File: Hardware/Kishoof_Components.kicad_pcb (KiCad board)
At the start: 4 copper layers, 70.8 x 100 mm, 98 parts, among them J1 Conn_01x12_Pin, J2 Conn_01x12_Pin, J3 Conn_01x12_Pin, J4 Conn_01x12_Pin, J5 Eurorack_10_pin_power, J6 SWD_Header, J7 Conn_01x02_Pin, U1 STM32H7B0VBTx, U2 PCM5100APW, U3 TPS561201, U4 LT1117-3.3, U5 MCP6002, U6 MX25LM51245G, U7 MCP6004, U8 TL072, Y1 8MHz 20pF

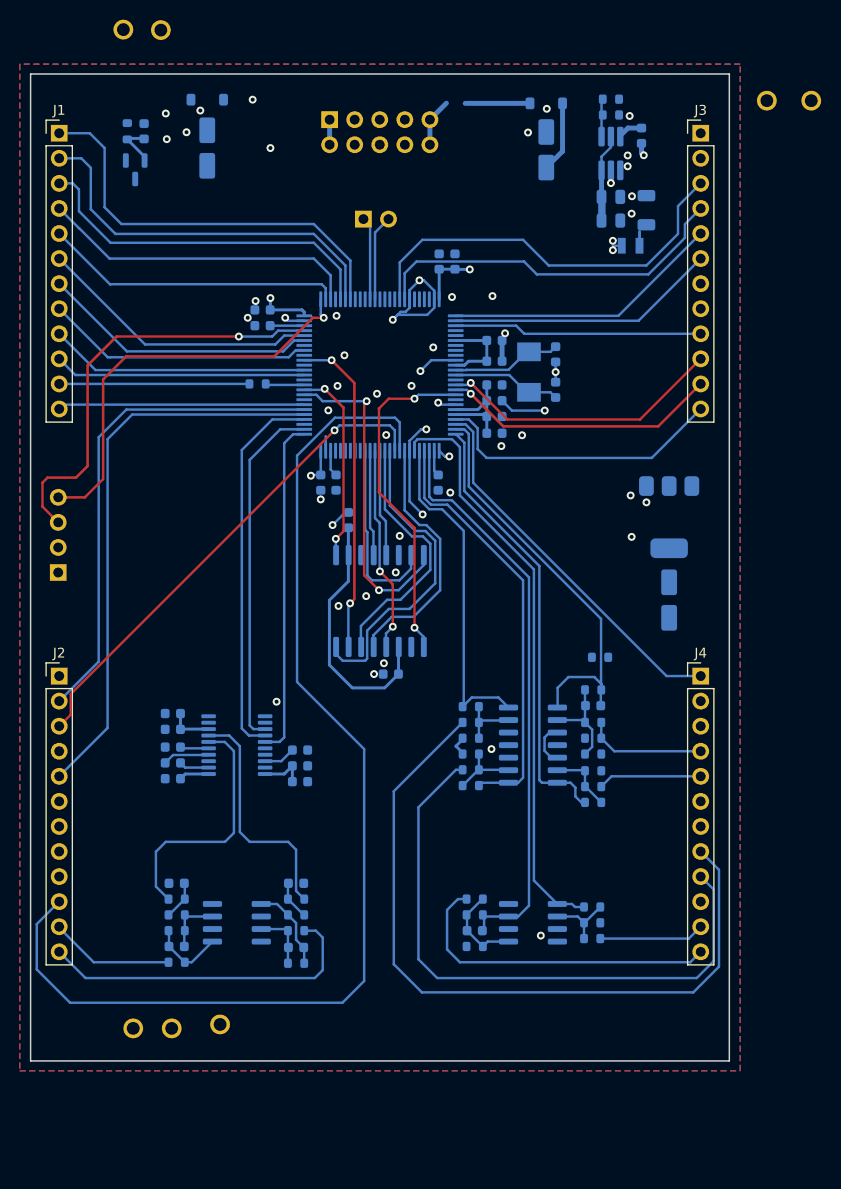
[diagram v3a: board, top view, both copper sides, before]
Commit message: First pass of component board routing complete
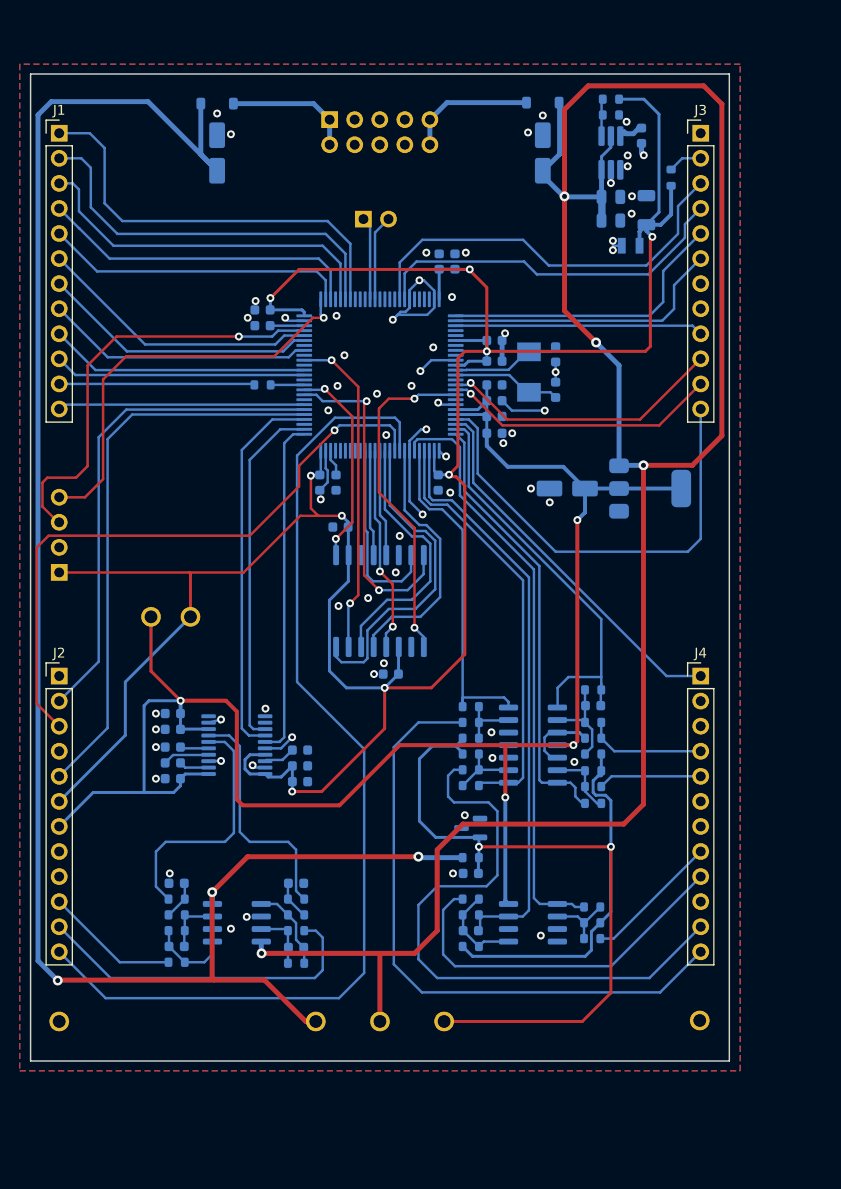
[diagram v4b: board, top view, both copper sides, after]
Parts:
- moved TP8 116.1 mm to (122.9, 134.9)
- moved TP3 105.9 mm to (84.0, 135.0)
- moved TP2 102.9 mm to (90.5, 135.0)
- moved TP7 98.9 mm to (97.0, 135.0)
- moved C36 82.2 mm to (99.7, 120.0), turned to 0 degrees
- moved R14 81.4 mm to (99.7, 118.4), turned to 0 degrees
- moved D3 74.9 mm to (99.7, 115.4), turned to 180 degrees
- moved R15 49.1 mm to (120.0, 49.5), turned to 90 degrees
- moved TP5 41.7 mm to (71.3, 94.0)
- moved TP6 41.7 mm to (67.3, 94.0)
- moved TP4 16.3 mm to (58.0, 135.0)
- moved C5 15.3 mm to (109.5, 81.0), turned to 180 degrees
- moved U4 3.48 mm to (117.9, 81.0), turned to 0 degrees
- moved C2 1.12 mm to (74.0, 47.0)
- moved D2 1.08 mm to (74.0, 42.0)
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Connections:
- J2 pad 1: unconnected-(J2-Pin_1-Pad1) -> GND
- J2 pad 10: /Warp_Type_Pot -> /Audio_Out_L
- J2 pad 11: /Audio_Out_L -> /Audio_Out_R
- J2 pad 12: /Audio_Out_R -> /Warp_Type_Pot
- J2 pad 4: unconnected-(J2-Pin_4-Pad4) -> GND
- J2 pad 6: GND -> +3.3V
- J2 pad 8: unconnected-(J2-Pin_8-Pad8) -> GND
- J2 pad 9: unconnected-(J2-Pin_9-Pad9) -> GND
- J3 pad 1: unconnected-(J3-Pin_1-Pad1) -> GND
- J3 pad 2: unconnected-(J3-Pin_2-Pad2) -> /LCD_Backlight
- J3 pad 7: unconnected-(J3-Pin_7-Pad7) -> GND
- J3 pad 8: unconnected-(J3-Pin_8-Pad8) -> GND
- J4 pad 10: unconnected-(J4-Pin_10-Pad10) -> GND
- J4 pad 11: /Wavetable_Pos_A_CV_In -> /Wavetable_Pos_B_CV_In
- J4 pad 12: /Pitch_CV_In -> /VCA_CV_In
- J4 pad 2: unconnected-(J4-Pin_2-Pad2) -> GND
- J4 pad 3: /LCD_Backlight -> GND
- J4 pad 6: +3.3V -> GND
- J4 pad 7: unconnected-(J4-Pin_7-Pad7) -> GND
- J4 pad 8: /VCA_CV_In -> /Wavetable_Pos_A_CV_In
- J4 pad 9: /Wavetable_Pos_B_CV_In -> /Pitch_CV_In
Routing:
- net +3.3V: track 58.2 -> 275.1 mm, vias 3 -> 9
- net +12V: track 15.7 -> 216.7 mm, vias 0 -> 4
- net -12V: track 0.00 -> 182.6 mm, vias 0 -> 3
- net +3.3VA: track 19.5 -> 177.7 mm, vias 0 -> 4
- net /-5V_REF: track 6.91 -> 105.8 mm, vias 0 -> 2
- net /Wavetable_Pos_B_Pot: track 29.7 -> 46.8 mm
- net /Wavetable_Pos_A_Pot: track 50.1 -> 63.9 mm
- net /VCA_CV_In: track 75.0 -> 64.0 mm
- net GND: track 50.1 -> 61.1 mm, vias 53 -> 63
- net /-12V_IN: track 2.54 -> 13.0 mm
- net /Warp_Type_Pot: track 114.4 -> 104.2 mm
- net /Pitch_CV_In: track 33.1 -> 37.3 mm
- net /LCD_Backlight: track 0.00 -> 3.47 mm
- net /Wavetable_Pos_A_CV_In: track 10.7 -> 13.8 mm
- net /Mode: track 28.3 -> 30.1 mm
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
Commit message: Cleaned up inter-board connectors
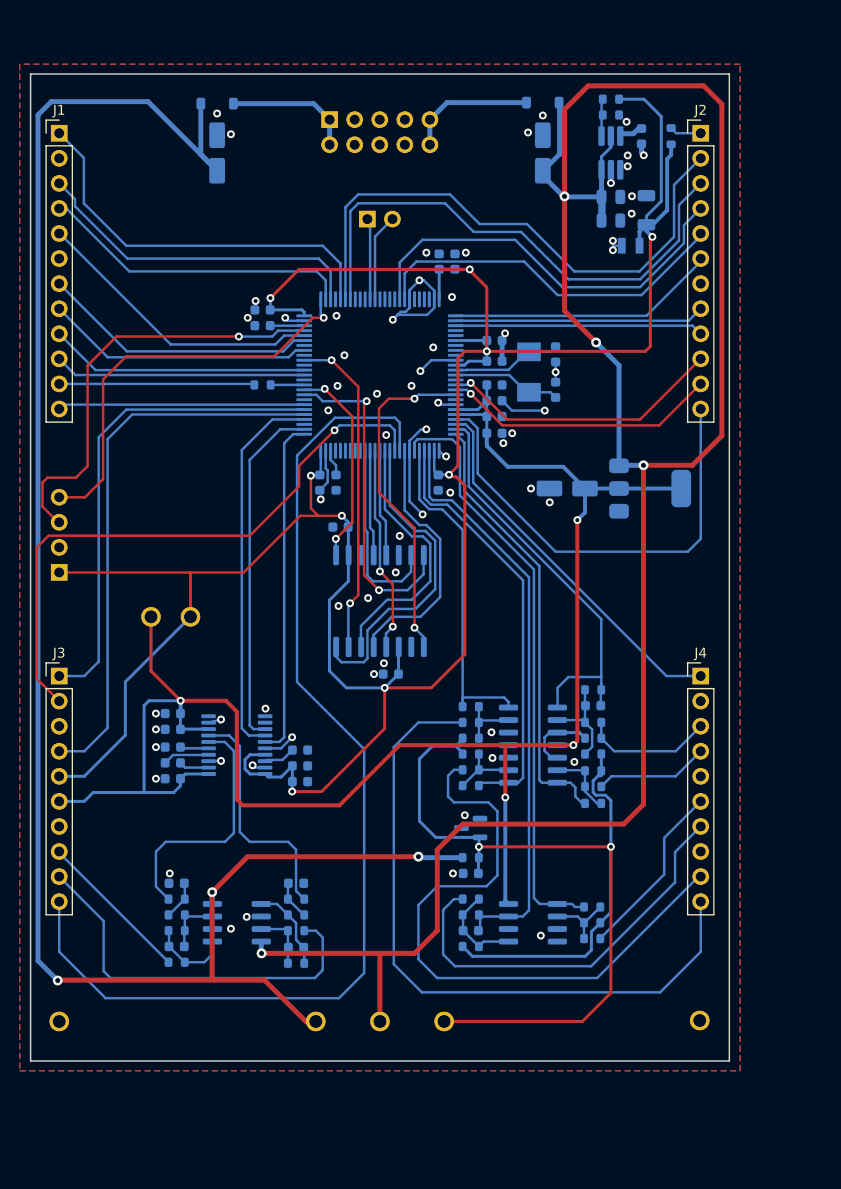
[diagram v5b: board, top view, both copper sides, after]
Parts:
- J3: renamed from J2; value Conn_01x12_Pin -> Conn_01x10_Pin; footprint Connector_PinHeader_2.54mm:PinHeader_1x12_P2.54mm_Vertical -> Connector_PinHeader_2.54mm:PinHeader_1x10_P2.54mm_Vertical
- J4: value Conn_01x12_Pin -> Conn_01x10_Pin; footprint Connector_PinHeader_2.54mm:PinHeader_1x12_P2.54mm_Vertical -> Connector_PinHeader_2.54mm:PinHeader_1x10_P2.54mm_Vertical
- moved R15 4.20 mm to (120.0, 45.3)
- moved J7 0.40 mm to (89.2, 53.7)
- renumbered J3 to J2
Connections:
- J1 pad 1: /Octave_Down -> /LCD_SPI3_MOSI
- J1 pad 2: /Octave_Up -> GND
- J1 pad 3: /LCD_SPI3_MOSI -> /LCD_SPI3_SCK
- J1 pad 4: /LCD_SPI3_SCK -> /LCD_SPI3_SS
- J1 pad 5: /LCD_SPI3_SS -> /USB_DP
- J1 pad 6: /USB_DP -> GND
- J2 pad 1: GND -> /LCD_Backlight
- J2 pad 2: /LCD_Backlight -> /Octave_Up
- J2 pad 3: /LCD_DC -> /Octave_Down
- J2 pad 4: /LCD_RESET -> /LCD_DC
- J2 pad 5: /Mode -> /LCD_RESET
- J2 pad 6: /Warp_Polarity_Btn -> /Mode
- J2 pad 8: GND -> /Warp_Polarity_Btn
- J3 pad 1: GND -> /ChB_RM
- J3 pad 10: /Audio_Out_L -> /Warp_Type_Pot
- J3 pad 2: /ChB_RM -> /Wavetable_Pos_A_Pot
- J3 pad 3: /Wavetable_Pos_A_Pot -> GND
- J3 pad 4: GND -> /ChB_Mix
- J3 pad 5: /ChB_Mix -> +3.3V
- J3 pad 6: +3.3V -> +3.3VA
- J3 pad 7: +3.3VA -> GND
- J3 pad 8: GND -> /Audio_Out_L
- J3 pad 9: GND -> /Audio_Out_R
- J4 pad 10: GND -> /VCA_CV_In
- J4 pad 3: GND -> /Ext_Audio_In
- J4 pad 4: /Ext_Audio_In -> /Warp_CV_In
- J4 pad 5: /Warp_CV_In -> GND
- J4 pad 6: GND -> /Wavetable_Pos_A_CV_In
- J4 pad 7: GND -> /Pitch_CV_In
- J4 pad 8: /Wavetable_Pos_A_CV_In -> GND
- J4 pad 9: /Pitch_CV_In -> /Wavetable_Pos_B_CV_In
- U1 pad 32: GND -> Net-(U1-PC4)
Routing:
- net /Octave_Up: track 40.0 -> 56.9 mm
- net /Octave_Down: track 43.0 -> 54.1 mm
- net Net-(U1-PC4): track 0.00 -> 10.2 mm, vias 0 -> 2
- net GND: track 61.1 -> 51.0 mm, vias 63 -> 61
- net /Audio_Out_R: track 34.7 -> 39.7 mm
- net /VCA_CV_In: track 64.0 -> 69.1 mm
- net /Warp_Type_Pot: track 104.2 -> 109.3 mm
- net /Wavetable_Pos_A_CV_In: track 13.8 -> 18.1 mm
- net /Pitch_CV_In: track 37.3 -> 41.2 mm
- net /LCD_SPI3_MOSI: track 36.8 -> 40.6 mm
- net /Warp_Polarity_Btn: track 28.8 -> 25.3 mm
- net +3.3V: track 275.1 -> 278.0 mm
- net /Mode: track 30.1 -> 27.4 mm
- net /Wavetable_Pos_A_Pot: track 63.9 -> 61.4 mm
- net /Audio_Out_L: track 13.6 -> 15.8 mm
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
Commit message: Control board routed; updated lcd riser
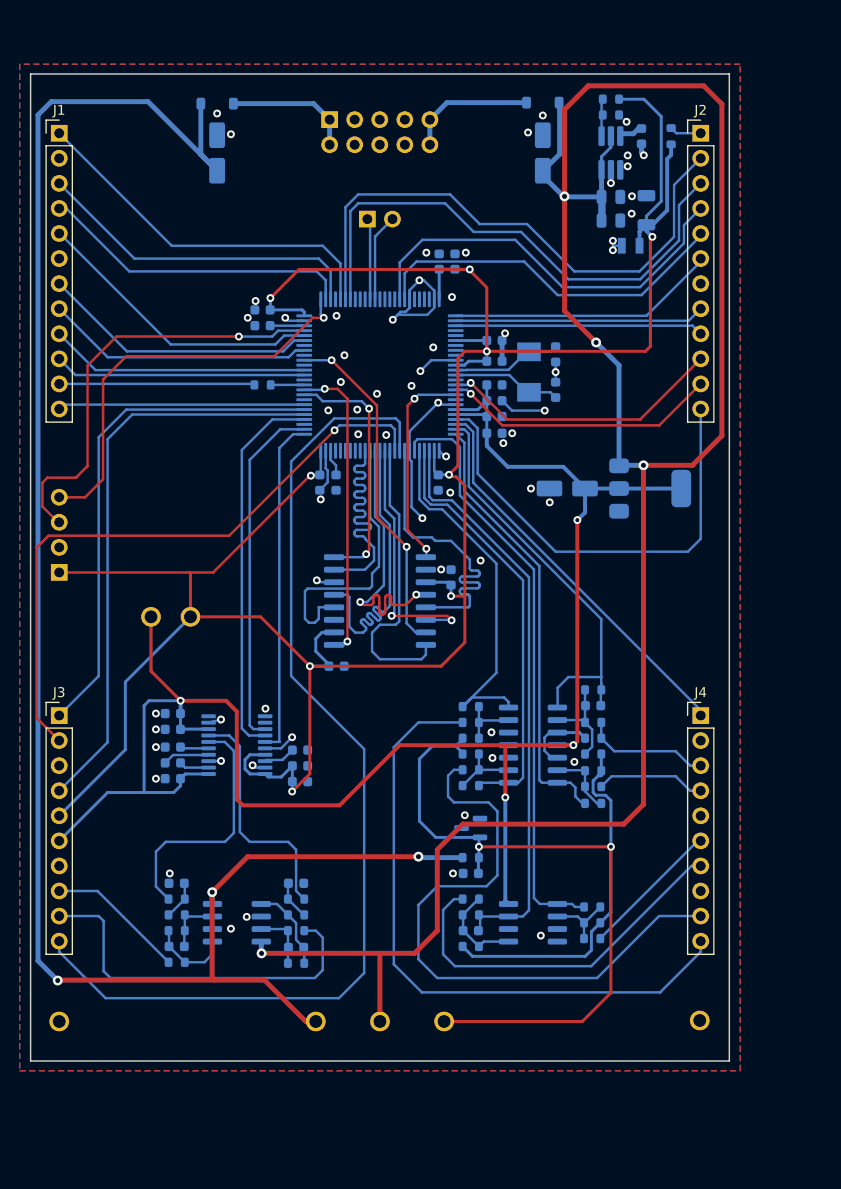
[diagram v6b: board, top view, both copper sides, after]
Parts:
- moved C34 12.3 mm to (97.7, 90.0), turned to 90 degrees
- moved C33 5.56 mm to (86.1, 99.0), turned to 0 degrees
- moved J3 4.00 mm to (58.0, 104.0)
- moved J4 4.00 mm to (123.0, 104.0)
- turned U6 to 0 degrees
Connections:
- U1 pad 32: Net-(U1-PC4) -> GND
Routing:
- net /OCTOSPIM_P1_IO5: track 10.8 -> 31.8 mm
- net /OCTOSPIM_P1_IO7: track 10.7 -> 28.6 mm
- net GND: track 51.0 -> 66.2 mm
- net /OCTOSPIM_P1_IO2: track 34.4 -> 21.5 mm
- net Net-(U1-PC4): track 10.2 -> 0.00 mm, vias 2 -> 0
- net /OCTOSPIM_P1_IO3: track 20.8 -> 30.9 mm
- net /OCTOSPIM_P1_IO6: track 20.9 -> 29.3 mm
- net /OCTOSPIM_P1_IO1: track 33.6 -> 25.4 mm
- net /OCTOSPIM_P1_NCS: track 19.5 -> 27.1 mm
- net /OCTOSPIM_P1_DQS: track 26.3 -> 31.9 mm
- net /VCA_CV_In: track 69.1 -> 65.1 mm
- net /Wavetable_Pos_A_CV_In: track 18.1 -> 14.3 mm
- net /Warp_Type_Pot: track 109.3 -> 105.7 mm
- net /Pitch_CV_In: track 41.2 -> 37.7 mm
- net /LCD_SPI3_MOSI: track 40.6 -> 37.6 mm
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
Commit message: PCBs v1.0 ordered
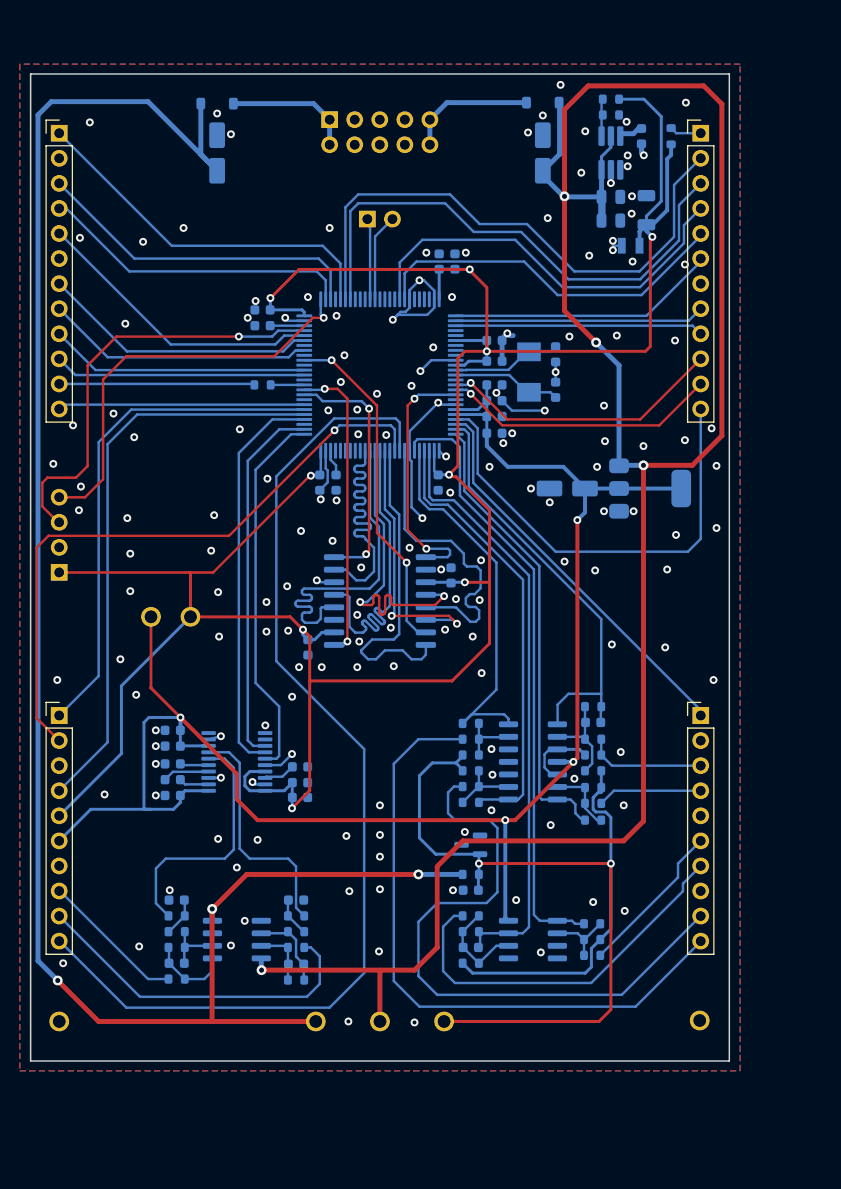
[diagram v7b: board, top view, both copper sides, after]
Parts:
- moved C33 3.47 mm to (83.2, 97.1), turned to -90 degrees
- moved C12 1.70 mm to (69.5, 105.5)
- moved C25 1.70 mm to (69.5, 110.5)
- moved C26 1.70 mm to (69.5, 108.9)
- moved C10 1.70 mm to (69.5, 112.1)
- moved C11 1.70 mm to (69.5, 107.1)
- moved R17 1.70 mm to (112.0, 128.3)
- moved R8 1.70 mm to (82.0, 130.8)
- moved C13 1.70 mm to (82.4, 110.8)
- moved C27 1.70 mm to (82.4, 109.2)
- moved C29 1.70 mm to (69.9, 122.7)
- moved C30 1.70 mm to (82.0, 122.7)
- moved C35 1.70 mm to (99.7, 127.5)
- moved C36 1.70 mm to (99.7, 121.7)
- moved C37 1.70 mm to (112.1, 104.7)
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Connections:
- C31 pad 2: Net-(U8A-+) -> Net-(U8A--)
- C32 pad 2: Net-(U8B-+) -> Net-(U8B--)
- C35 pad 2: Net-(U5B-+) -> Net-(U5B--)
- R22 pad 1: Net-(U5B-+) -> Net-(U5B--)
- R23 pad 1: Net-(U5B-+) -> Net-(U5B--)
- R24 pad 2: Net-(U5B-+) -> Net-(U5B--)
- R5 pad 1: Net-(U8A-+) -> Net-(U8A--)
- R6 pad 1: Net-(U8B-+) -> Net-(U8B--)
- R7 pad 2: Net-(U8A-+) -> Net-(U8A--)
- R8 pad 2: Net-(U8B-+) -> Net-(U8B--)
- U5 pad 5: Net-(U5B-+) -> GND
- U5 pad 6: GND -> Net-(U5B--)
- U8 pad 2: GND -> Net-(U8A--)
- U8 pad 3: Net-(U8A-+) -> GND
- U8 pad 5: Net-(U8B-+) -> GND
- U8 pad 6: GND -> Net-(U8B--)
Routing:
- net Net-(U5B--): track 0.00 -> 9.93 mm
- net Net-(U5B-+): track 9.00 -> 0.00 mm
- net Net-(U8B-+): track 8.74 -> 0.00 mm
- net Net-(U8B--): track 0.00 -> 8.35 mm
- net +3.3VA: track 178.3 -> 171.3 mm
- net Net-(U8A-+): track 6.09 -> 0.00 mm
- net Net-(U8A--): track 0.00 -> 6.09 mm
- net +3.3V: track 276.9 -> 282.4 mm
- net /OCTOSPIM_P1_IO7: track 28.6 -> 33.7 mm
- net /OCTOSPIM_P1_IO2: track 21.5 -> 26.1 mm
- net /OCTOSPIM_P1_IO6: track 29.3 -> 33.0 mm
- net /DAC_LRCLK: track 34.4 -> 38.0 mm
- net /Audio_Out_R: track 38.1 -> 35.1 mm
- net /OCTOSPIM_P1_CLK: track 29.8 -> 32.5 mm
- net -12V: track 182.6 -> 185.0 mm
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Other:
- board text added: "Kishoof v1.0 2024 Mountjoy Modular and Tal Shoshani"
